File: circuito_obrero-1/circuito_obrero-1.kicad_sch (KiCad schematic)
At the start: 49 parts, among them J1 Conn_01x03_Pin, J10 Conn_01x05, J2 Conn_01x03_Pin, J3 Conn_01x03_Pin, J4 Conn_01x03_Pin, J5 Conn_01x03_Pin, J6 Conn_01x03_Pin, J7 Conn_01x03_Pin, J8 Conn_01x03_Pin, J9 Conn_01x05, U1 74HC165, U2 74HC165, U3 74HC165

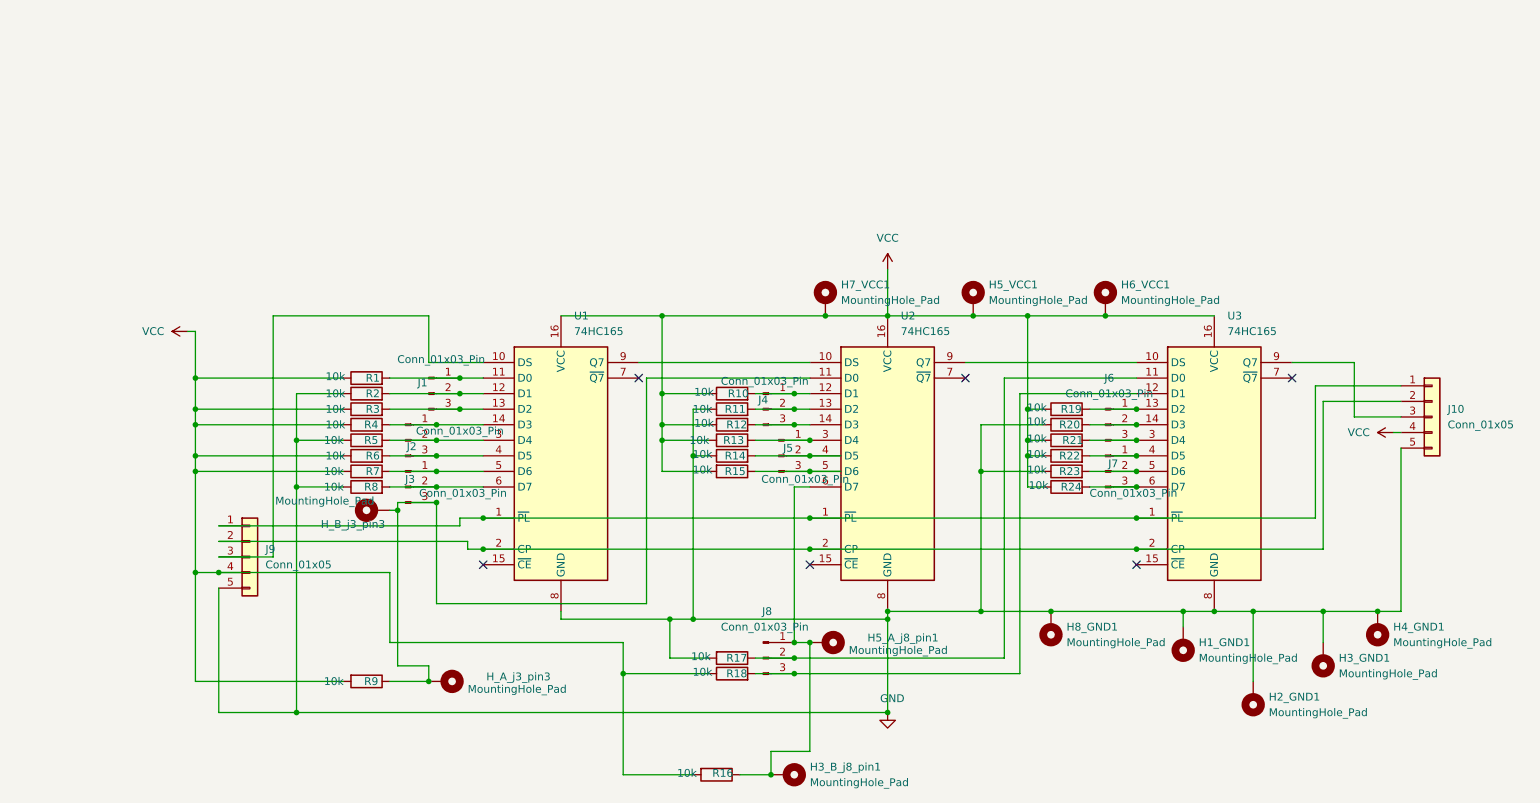
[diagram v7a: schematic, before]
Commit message: recableando mas prolijo
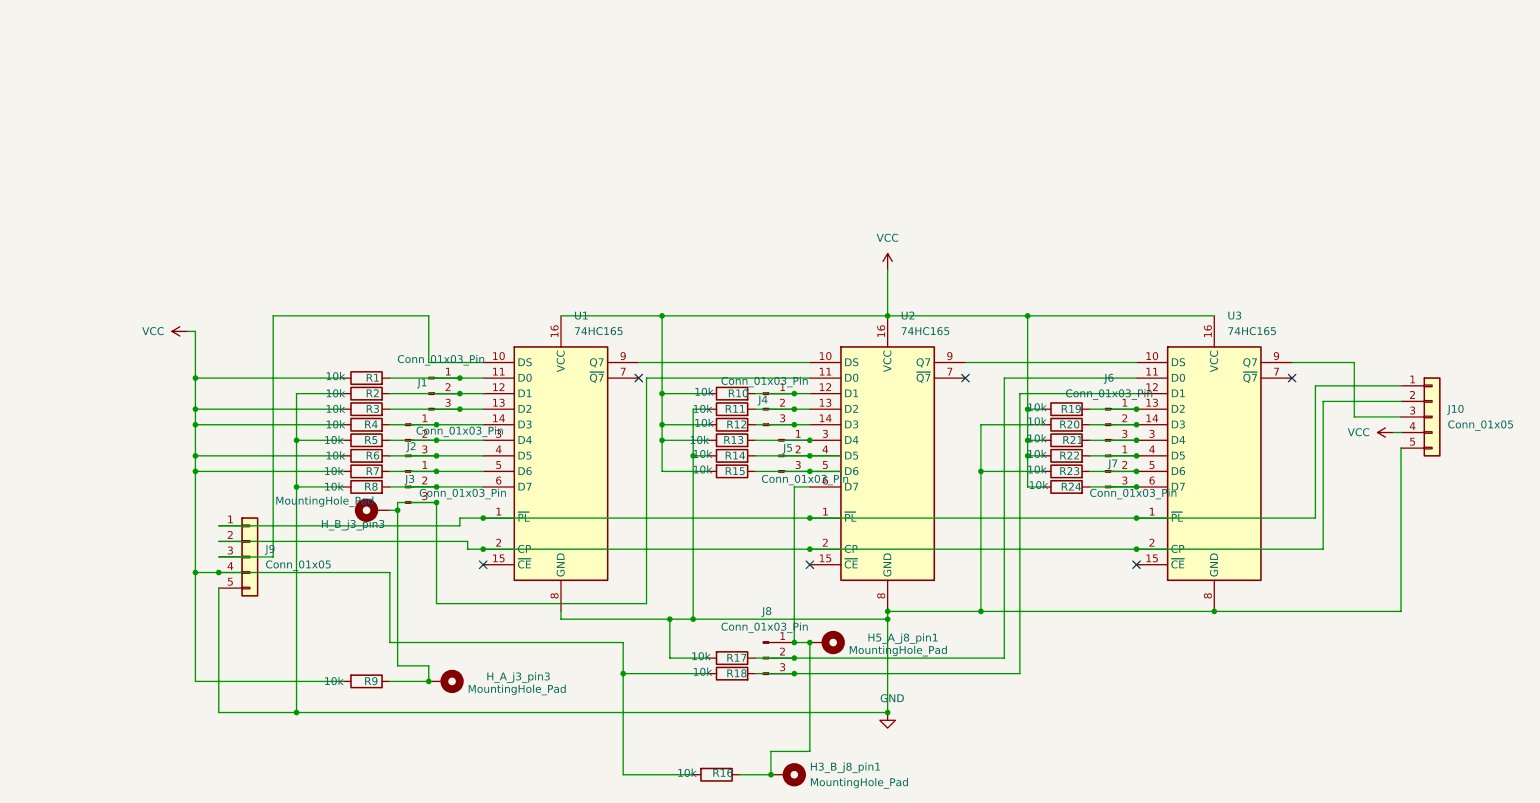
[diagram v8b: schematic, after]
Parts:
- removed H1_GND1, H2_GND1, H3_GND1, H4_GND1, H5_VCC1, H6_VCC1, H7_VCC1, H8_GND1: MountingHole_Pad, MountingHole:MountingHole_2.2mm_M2_DIN965_Pad_TopOnly, symbol Mechanical:MountingHole_Pad
